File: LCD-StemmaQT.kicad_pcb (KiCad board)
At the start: 2 copper layers, 41.5 x 19 mm, 19 parts, among them J101 Conn_01x04, J102 Conn_01x16, J103 Conn_01x02, Q101 MMBT3904, U101 PCF8574TS

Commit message: Non functional corrections on PCB
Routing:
- net /DB7: track 3.99 -> 5.06 mm
- net /DB4: track 4.13 -> 4.82 mm
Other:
- board text added: "V${REVISION} ${ISSUE_DATE}"
- board text removed: "V1.0.0 23.12.2022"
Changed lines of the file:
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@@
   (title_block
     (title "LCD backplate with Stemma QT connector")
-    (date "2022-12-23")
-    (rev "1.0.0")
+    (date "23.12.2022")
+    (rev "1.0.1")
     (company "Resterampe Berlin")
     (comment 3 "https://creativecommons.org/licenses/by-nc/4.0")
@@
   )
   (gr_rect locked (start 135.1 82.525) (end 176.6 101.525) (layer "Edge.Cuts") (width 0.1) (fill none))
-  (gr_text "A2" (at 154.3 98.8 90) (layer "F.Cu")
-    (effects (font (size 1.2 1.2) (thickness 0.2)))
-  )
   (gr_text "A1" (at 149.975 98.625 90) (layer "F.SilkS")
     (effects (font (size 1.2 1.2) (thickness 0.2)))
@@
     (effects (font (size 1.2 1.2) (thickness 0.2)))
   )
-  (gr_text "V1.0.0\n23.12.2022" (at 159.9 99.475) (layer "F.SilkS")
+  (gr_text "A2" (at 154.3 98.8 90) (layer "F.SilkS")
+    (effects (font (size 1.2 1.2) (thickness 0.2)))
+  )
+  (gr_text "V${REVISION}\n${ISSUE_DATE}" (at 159.9 99.475) (layer "F.SilkS")
     (effects (font (size 1 1) (thickness 0.15)))
   )
@@
   (segment (start 149.6 86.45) (end 150.025 86.025) (width 0.25) (layer "F.Cu") (net 17))
   (segment (start 149.6 87.2) (end 149.6 86.45) (width 0.25) (layer "F.Cu") (net 17))
-  (segment (start 149.25 84.25) (end 149.5 84.25) (width 0.25) (layer "F.Cu") (net 19))
-  (segment (start 147 86.5) (end 149.25 84.25) (width 0.25) (layer "F.Cu") (net 19))
+  (segment (start 148.875 86.05) (end 149.5 85.425) (width 0.25) (layer "F.Cu") (net 19))
   (segment (start 147 87.2) (end 147 86.5) (width 0.25) (layer "F.Cu") (net 19))
-  (segment (start 146.35 84.86) (end 146.96 84.25) (width 0.25) (layer "F.Cu") (net 20))
-  (segment (start 146.35 87.2) (end 146.35 84.86) (width 0.25) (layer "F.Cu") (net 20))
-  (segment (start 145.05 84.88) (end 144.42 84.25) (width 0.25) (layer "F.Cu") (net 22))
-  (segment (start 145.05 87.2) (end 145.05 84.88) (width 0.25) (layer "F.Cu") (net 22))
-  (segment (start 144.4 87.2) (end 144.4 86.77) (width 0.25) (layer "F.Cu") (net 23))
-  (segment (start 144.4 86.77) (end 141.88 84.25) (width 0.25) (layer "F.Cu") (net 23))
+  (segment (start 147.45 86.05) (end 148.875 86.05) (width 0.25) (layer "F.Cu") (net 19))
+  (segment (start 149.5 85.425) (end 149.5 84.25) (width 0.25) (layer "F.Cu") (net 19))
+  (segment (start 147 86.5) (end 147.45 86.05) (width 0.25) (layer "F.Cu") (net 19))
+  (segment (start 146.35 86.513604) (end 146.96 85.903604) (width 0.25) (layer "F.Cu") (net 20))
+  (segment (start 146.96 85.903604) (end 146.96 84.25) (width 0.25) (layer "F.Cu") (net 20))
+  (segment (start 146.35 87.2) (end 146.35 86.513604) (width 0.25) (layer "F.Cu") (net 20))
+  (segment (start 144.42 85.655) (end 144.42 84.25) (width 0.25) (layer "F.Cu") (net 22))
+  (segment (start 145.05 86.325) (end 144.4 85.675) (width 0.25) (layer "F.Cu") (net 22))
+  (segment (start 144.4 85.675) (end 144.42 85.655) (width 0.25) (layer "F.Cu") (net 22))
+  (segment (start 145.05 87.2) (end 145.05 86.325) (width 0.25) (layer "F.Cu") (net 22))
+  (segment (start 142.35 86.075) (end 141.88 85.605) (width 0.25) (layer "F.Cu") (net 23))
+  (segment (start 141.88 85.605) (end 141.88 84.25) (width 0.25) (layer "F.Cu") (net 23))
+  (segment (start 144.163604 86.075) (end 142.35 86.075) (width 0.25) (layer "F.Cu") (net 23))
+  (segment (start 144.4 87.2) (end 144.4 86.311396) (width 0.25) (layer "F.Cu") (net 23))
+  (segment (start 144.4 86.311396) (end 144.163604 86.075) (width 0.25) (layer "F.Cu") (net 23))
   (segment (start 137.9 94.825) (end 137.9 96.643343) (width 0.4) (layer "B.Cu") (net 28))
   (segment (start 137.9 96.643343) (end 139.575 98.318343) (width 0.4) (layer "B.Cu") (net 28))

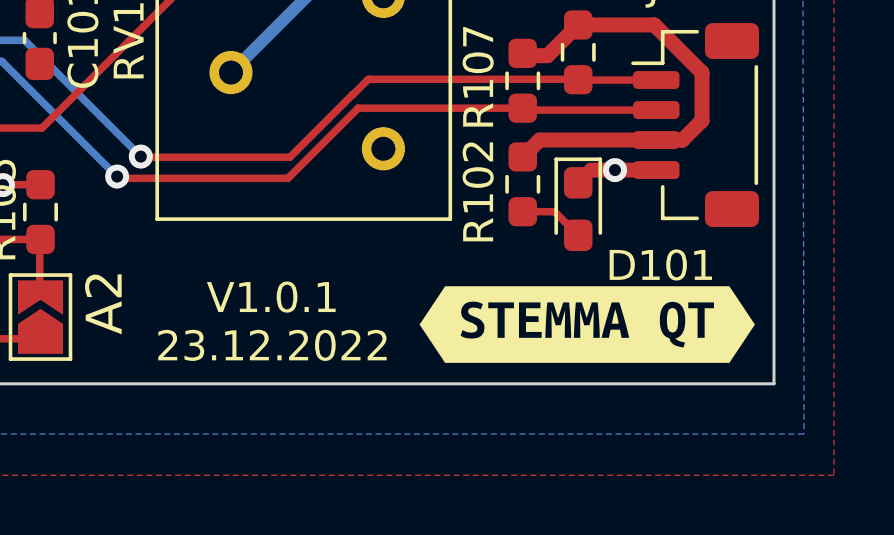
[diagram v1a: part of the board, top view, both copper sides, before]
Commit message: added StemmaQT logo on PCB
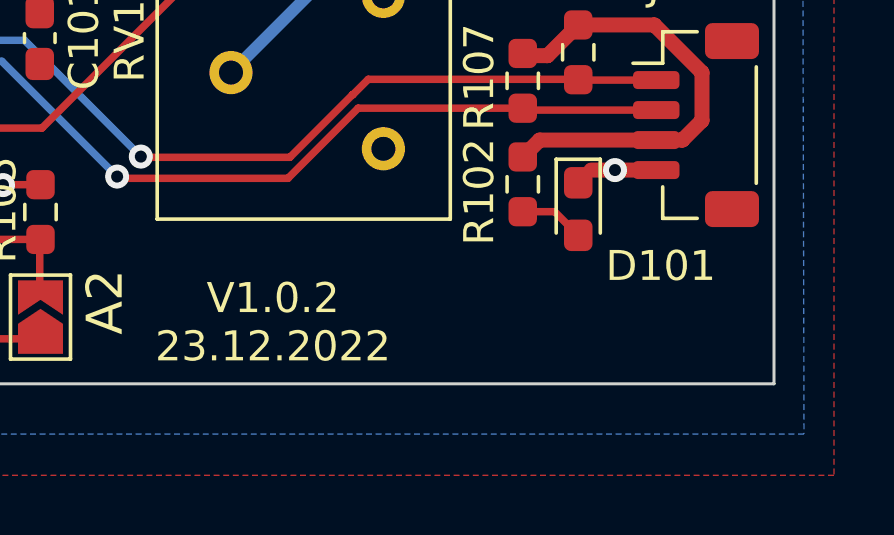
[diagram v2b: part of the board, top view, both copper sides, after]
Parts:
- removed kibuzzard-63A61B1D: G***, kibuzzard-63A61B1D

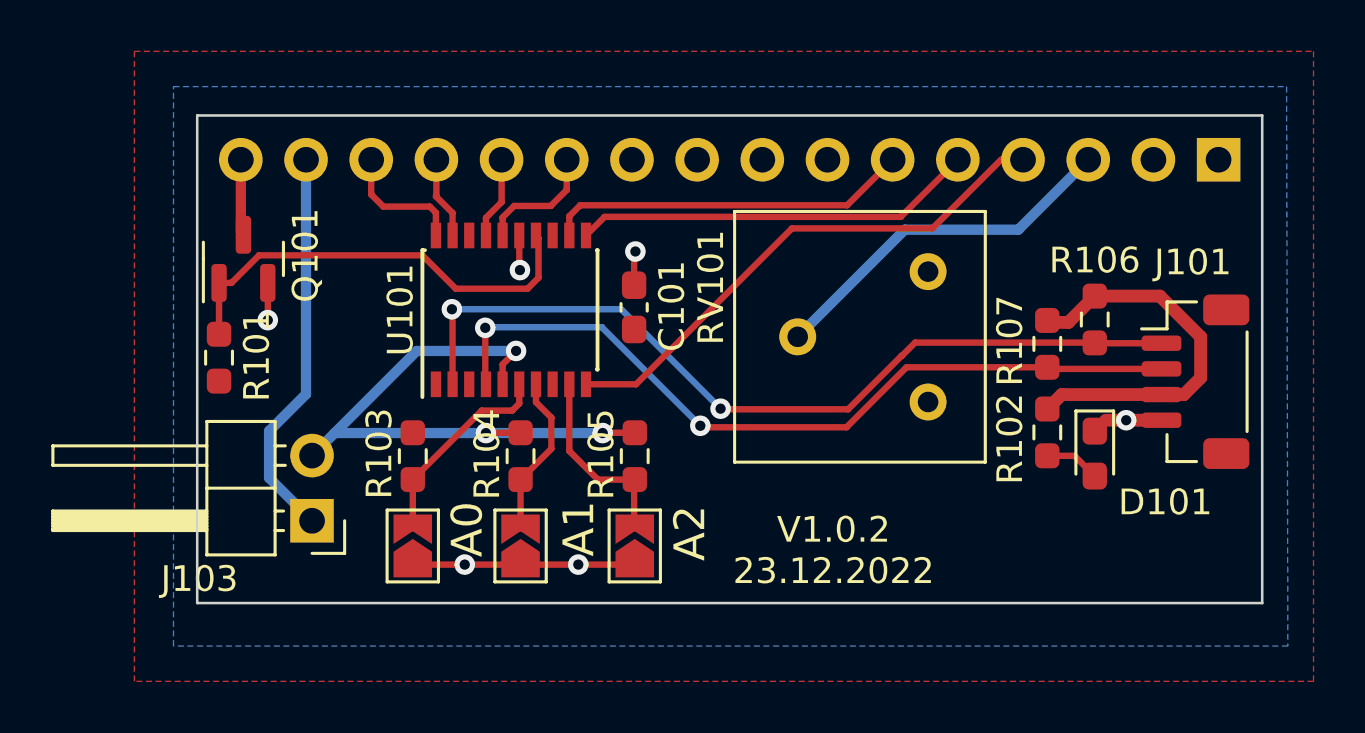
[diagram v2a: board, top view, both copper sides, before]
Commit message: Stemma QT footprint corrected
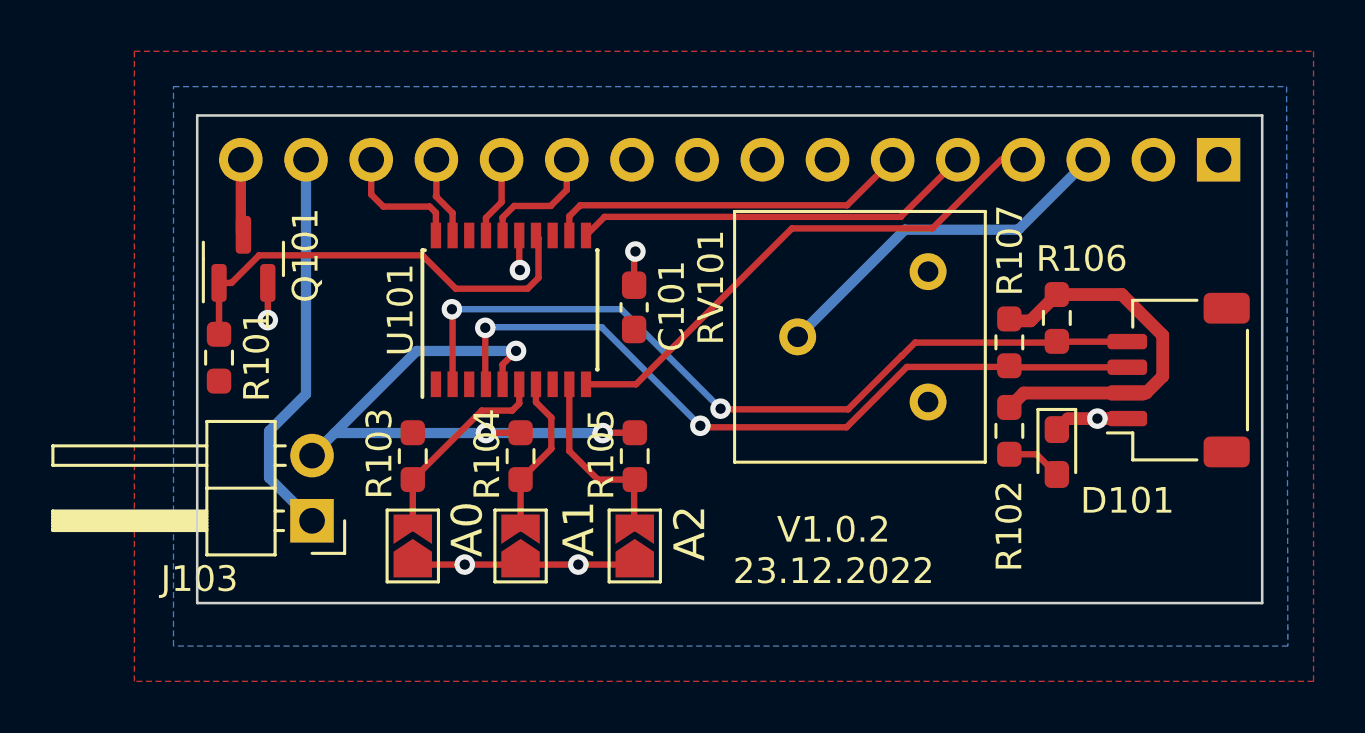
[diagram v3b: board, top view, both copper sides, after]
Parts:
- J101: value Conn_01x04 -> StemmaQT; footprint Connector_JST:JST_SH_BM04B-SRSS-TB_1x04-1MP_P1.00mm_Vertical -> Connector_JST:JST_SH_SM04B-SRSS-TB_1x04-1MP_P1.00mm_Horizontal
- J102: value Conn_01x16 -> LCD
- J103: value Conn_01x02 -> BL enable
- JP101: value SolderJumper_2_Open -> A0
- JP102: value SolderJumper_2_Open -> A1
- JP103: value SolderJumper_2_Open -> A2
- moved D101 1.48 mm to (168.6, 95.6)
- moved R102 1.48 mm to (166.7, 94.8)
- moved R106 1.48 mm to (168.6, 90.4)
- moved R107 1.48 mm to (166.7, 91.4)
- moved J101 0.66 mm to (173.3, 92.8), turned to 90 degrees
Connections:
- J101 pad 1: /SCL -> GND
- J101 pad 2: /SDA -> VCC
- J101 pad 3: VCC -> /SDA
- J101 pad 4: GND -> /SCL
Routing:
- net /SCL: track 33.3 -> 31.8 mm
- net /SDA: track 31.1 -> 29.7 mm

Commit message: Added second StemmaQT port
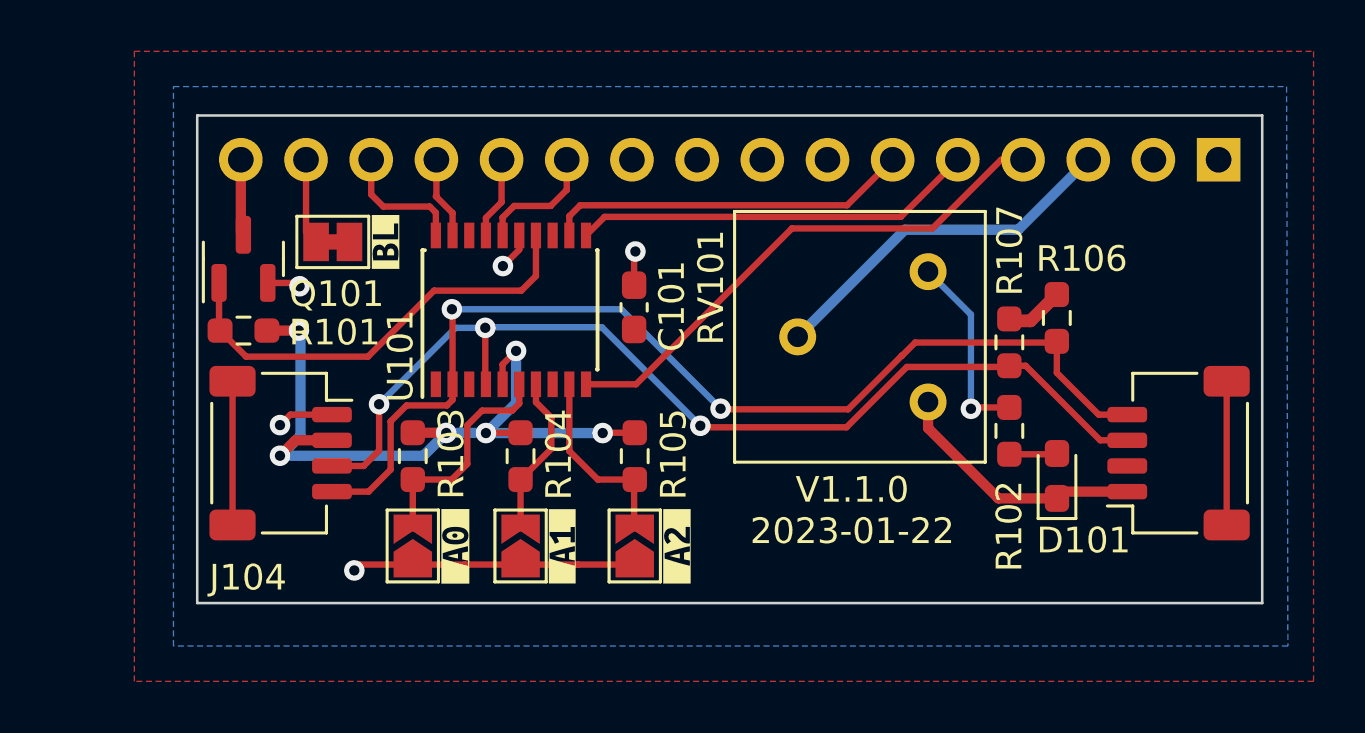
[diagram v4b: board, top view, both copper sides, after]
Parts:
- removed J103: BL enable, Connector_PinHeader_2.54mm:PinHeader_1x02_P2.54mm_Horizontal
- added J104: StemmaQT, Connector_JST:JST_SH_SM04B-SRSS-TB_1x04-1MP_P1.00mm_Horizontal, F.Cu at (138.4, 95.7)
- added JP104: BL, Jumper:SolderJumper-2_P1.3mm_Bridged_Pad1.0x1.5mm, F.Cu at (140.4, 87.5)
- added kibuzzard-63CD50DB: G***, kibuzzard-63CD50DB, F.Cu at (142.4, 87.5)
- added kibuzzard-63CD512B: G***, kibuzzard-63CD512B, F.Cu at (145.2, 99.3)
- added kibuzzard-63CD5133: G***, kibuzzard-63CD5133, F.Cu at (149.3, 99.3)
- added kibuzzard-63CD5139: G***, kibuzzard-63CD5139, F.Cu at (153.8, 99.3)
- moved J101 2.85 mm to (173.3, 95.7)
- moved R101 1.42 mm to (136.9, 90.9), turned to 180 degrees
- moved D101 0.93 mm to (168.6, 96.6), turned to 90 degrees
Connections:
- J101 pad MP: (no net) -> unconnected-(J101-PadMP)
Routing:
- net /LCD_A: track 15.4 -> 3.37 mm
- net GND: track 15.7 -> 27.3 mm, vias 6 -> 5
- net /SDA: track 29.7 -> 40.3 mm, vias 2 -> 3
- net /SCL: track 31.8 -> 41.8 mm
- net unconnected-(J104-PadMP): track 0.00 -> 5.60 mm
- net unconnected-(J101-PadMP): track 0.00 -> 5.60 mm
- net /A0: track 7.99 -> 8.87 mm
- net VCC: vias 3 -> 7
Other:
- board text removed: "A0"
- board text removed: "A1"
- board text removed: "A2"
